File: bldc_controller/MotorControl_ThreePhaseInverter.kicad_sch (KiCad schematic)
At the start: 42 parts, among them J11 Phase A, J12 Phase B, J13 Phase C

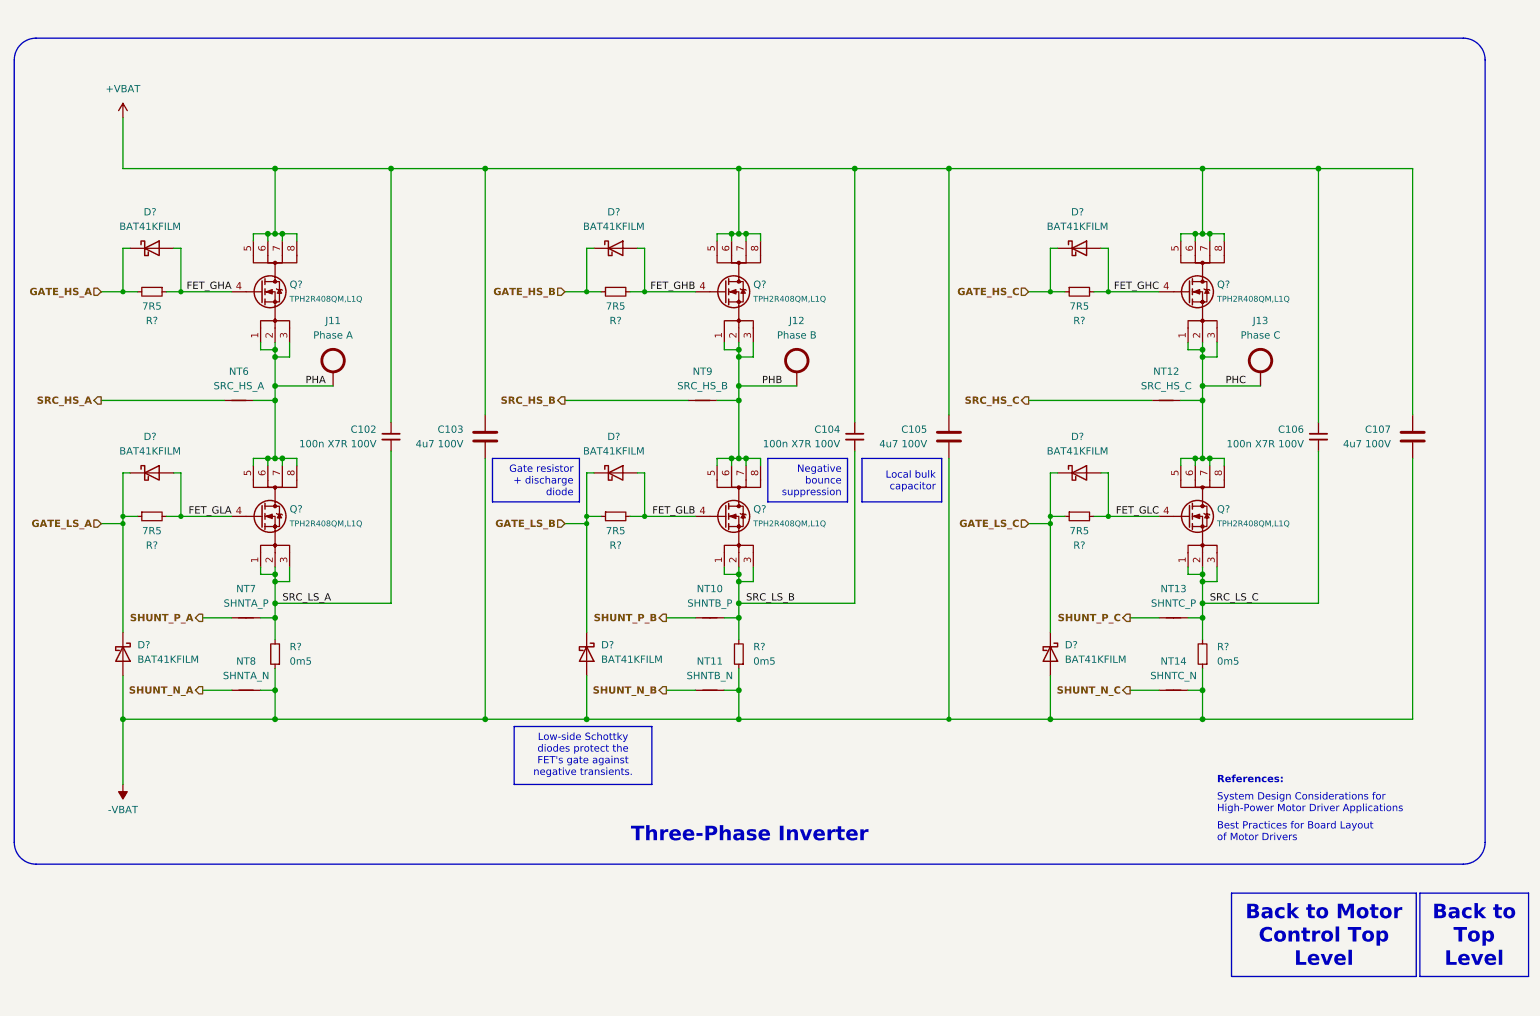
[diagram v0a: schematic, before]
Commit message: added IPC-7351 compliant footprints and started routing
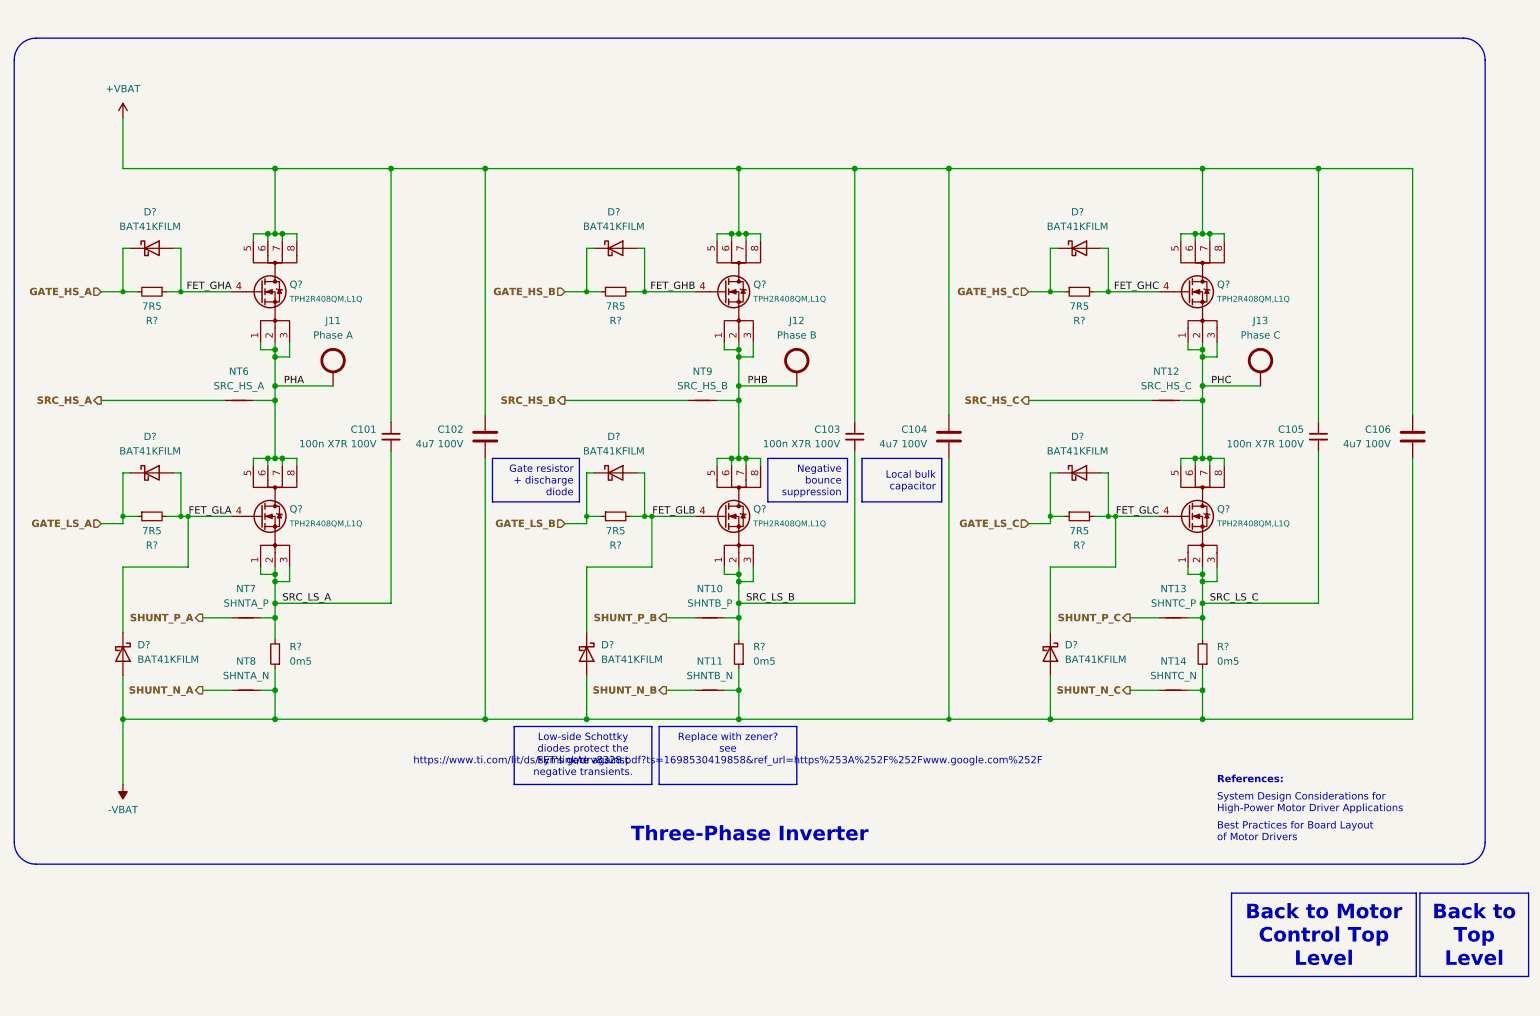
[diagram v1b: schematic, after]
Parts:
- C101: renamed from C102; footprint (none) -> 0_capacitor_smd:C_1206_3216_DensityHighest
- C102: renamed from C103; footprint Capacitor_SMD:C_1206_3216Metric -> 0_capacitor_smd:C_1206_3216_DensityHighest
- C103: renamed from C104; footprint (none) -> 0_capacitor_smd:C_1206_3216_DensityHighest
- C104: renamed from C105; footprint Capacitor_SMD:C_1206_3216Metric -> 0_capacitor_smd:C_1206_3216_DensityHighest
- C105: renamed from C106; footprint (none) -> 0_capacitor_smd:C_1206_3216_DensityHighest
- C106: renamed from C107; footprint Capacitor_SMD:C_1206_3216Metric -> 0_capacitor_smd:C_1206_3216_DensityHighest
- NT10, NT11, NT13, NT14, NT7, NT8: footprint NetTie:NetTie-2_SMD_Pad0.5mm -> 0_net_tie:NetTie-2_SMD_Pad0.2mm
- NT12, NT6, NT9: footprint NetTie:NetTie-2_SMD_Pad0.5mm -> 0_net_tie:NetTie-2_SMD_Pad0.4mm
- R? (x3): footprint Resistor_SMD:R_1206_3216Metric -> 0_resistor_smd:R_1206_3216_DensityHigh
- R? (x6): footprint Resistor_SMD:R_0805_2012Metric -> 0_resistor_smd:R_0805_2012_DensityHigh
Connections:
- net FET_GLA: now also D?.1 (K)
- net FET_GLB: now also D?.1 (K)
- net FET_GLC: now also D?.1 (K)
- net GATE_LS_A: no longer D?.1 (K)
- net GATE_LS_B: no longer D?.1 (K)
- net GATE_LS_C: no longer D?.1 (K)

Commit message: some progress on the pcb
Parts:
- C103: footprint 0_capacitor_smd:C_1206_3216_DensityHighest -> 0_capacitor_smd:C_0805_2012_DensityHigh
- D?: footprint Diode_SMD:D_SOD-523 -> 0_diode_smd:D_SOD-523_Spaced
- J11, J12, J13: footprint MountingHole:MountingHole_5mm_Pad_Via -> 0_pad:Pad_Square_Vias_6.5x6.5mm
- NT12, NT6, NT9: footprint 0_net_tie:NetTie-2_SMD_Pad0.4mm -> 0_net_tie:NetTie-2_SMD_Pad0.3mm
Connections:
- net -VBAT renamed GND
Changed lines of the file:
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@@
       (effects (font (size 1.27 1.27)))
     )
-    (property "Footprint" "0_net_tie:NetTie-2_SMD_Pad0.4mm" (at 220.98 80.01 0)
+    (property "Footprint" "0_net_tie:NetTie-2_SMD_Pad0.3mm" (at 220.98 80.01 0)
       (effects (font (size 1.27 1.27)) hide)
     )
@@
       (effects (font (size 1.27 1.27)))
     )
-    (property "Footprint" "0_net_tie:NetTie-2_SMD_Pad0.4mm" (at 58.42 80.01 0)
+    (property "Footprint" "0_net_tie:NetTie-2_SMD_Pad0.3mm" (at 58.42 80.01 0)
       (effects (font (size 1.27 1.27)) hide)
     )
@@
       (effects (font (size 1.27 1.27)) (justify left))
     )
-    (property "Footprint" "0_capacitor_smd:C_1206_3216_DensityHighest" (at 166.37 86.36 0)
+    (property "Footprint" "0_capacitor_smd:C_0805_2012_DensityHigh" (at 166.37 86.36 0)
       (effects (font (size 1.27 1.27)) hide)
     )
@@
     )
   )
-  (symbol (lib_id "0_power_symbols:-VBAT") (at 38.1 147.32 180) (unit 1)
-    (in_bom yes) (on_board yes) (dnp no) (fields_autoplaced)
-    (property "Reference" "#PWR?" (at 38.1 149.86 0)
-      (effects (font (size 1.27 1.27)) hide)
-    )
-    (property "Value" "-VBAT" (at 38.1 151.765 0)
+  (symbol (lib_id "0_diode:BAT41KFILM") (at 205.74 53.34 0) (unit 1)
+    (in_bom yes) (on_board yes) (dnp no) (fields_autoplaced)
+    (property "Reference" "D?" (at 205.4225 46.99 0)
+      (effects (font (size 1.27 1.27)))
+    )
+    (property "Value" "BAT41KFILM" (at 205.4225 49.53 0)
+      (effects (font (size 1.27 1.27)))
+    )
+    (property "Footprint" "Diode_SMD:D_SOD-523" (at 205.74 57.785 0)
+      (effects (font (size 1.27 1.27)) hide)
+    )
+    (property "Datasheet" "https://www.mouser.ch/datasheet/2/389/bat41-1848934.pdf" (at 205.74 53.34 0)
+      (effects (font (size 1.27 1.27)) hide)
+    )
+    (pin "1")
+    (pin "2")
+    (instances
+      (project "bldc_controller"
+        (path "/0650c7a8-acba-429c-9f8e-eec0baf0bc1c/a6223e2e-2896-4182-b4ad-55a63bc87f3d"
+          (reference "D?") (unit 1)
+        )
+        (path "/0650c7a8-acba-429c-9f8e-eec0baf0bc1c/a6223e2e-2896-4182-b4ad-55a63bc87f3d/4a9c9b06-3536-46ef-a76d-6cac03a1fe38"
+          (reference "D13") (unit 1)
+        )
+      )
+    )
+  )
+  (symbol (lib_id "0_diode:BAT41KFILM") (at 200.66 124.46 270) (unit 1)
+    (in_bom yes) (on_board yes) (dnp no) (fields_autoplaced)
+    (property "Reference" "D?" (at 203.2 122.8725 90)
+      (effects (font (size 1.27 1.27)) (justify left))
+    )
+    (property "Value" "BAT41KFILM" (at 203.2 125.4125 90)
+      (effects (font (size 1.27 1.27)) (justify left))
+    )
+    (property "Footprint" "Diode_SMD:D_SOD-523" (at 196.215 124.46 0)
+      (effects (font (size 1.27 1.27)) hide)
+    )
+    (property "Datasheet" "https://www.mouser.ch/datasheet/2/389/bat41-1848934.pdf" (at 200.66 124.46 0)
+      (effects (font (size 1.27 1.27)) hide)
+    )
+    (pin "1")
+    (pin "2")
+    (instances
+      (project "bldc_controller"
+        (path "/0650c7a8-acba-429c-9f8e-eec0baf0bc1c/a6223e2e-2896-4182-b4ad-55a63bc87f3d"
+          (reference "D?") (unit 1)
+        )
+        (path "/0650c7a8-acba-429c-9f8e-eec0baf0bc1c/a6223e2e-2896-4182-b4ad-55a63bc87f3d/4a9c9b06-3536-46ef-a76d-6cac03a1fe38"
+          (reference "D12") (unit 1)
+        )
+      )
+    )
+  )
+  (symbol (lib_id "Device:R_Small") (at 205.74 100.33 90) (mirror x) (unit 1)
+    (in_bom yes) (on_board yes) (dnp no)
+    (property "Reference" "R?" (at 205.74 105.41 90)
+      (effects (font (size 1.27 1.27)))
+    )
+    (property "Value" "7R5" (at 205.74 102.87 90)
+      (effects (font (size 1.27 1.27)))
+    )
+    (property "Footprint" "0_resistor_smd:R_0805_2012_DensityHigh" (at 205.74 100.33 0)
+      (effects (font (size 1.27 1.27)) hide)
+    )
+    (property "Datasheet" "~" (at 205.74 100.33 0)
+      (effects (font (size 1.27 1.27)) hide)
+    )
+    (pin "1")
+    (pin "2")
+    (instances
+      (project "bldc_controller"
+        (path "/0650c7a8-acba-429c-9f8e-eec0baf0bc1c/a6223e2e-2896-4182-b4ad-55a63bc87f3d"
+          (reference "R?") (unit 1)
+        )
+        (path "/0650c7a8-acba-429c-9f8e-eec0baf0bc1c/a6223e2e-2896-4182-b4ad-55a63bc87f3d/4a9c9b06-3536-46ef-a76d-6cac03a1fe38"
+          (reference "R39") (unit 1)
+        )
+      )
+    )
+  )
+  (symbol (lib_id "power:GND") (at 38.1 147.32 0) (unit 1)
+    (in_bom yes) (on_board yes) (dnp no) (fields_autoplaced)
+    (property "Reference" "#PWR07" (at 38.1 153.67 0)
+      (effects (font (size 1.27 1.27)) hide)
+    )
+    (property "Value" "GND" (at 38.1 152.4 0)
       (effects (font (size 1.27 1.27)))
     )
@@
     (instances
       (project "bldc_controller"
-        (path "/0650c7a8-acba-429c-9f8e-eec0baf0bc1c/a6223e2e-2896-4182-b4ad-55a63bc87f3d"
-          (reference "#PWR?") (unit 1)
+        (path "/0650c7a8-acba-429c-9f8e-eec0baf0bc1c/b89a7d22-bda3-4776-b5ce-8f6b0eb8f2a5"
+          (reference "#PWR07") (unit 1)
         )
         (path "/0650c7a8-acba-429c-9f8e-eec0baf0bc1c/a6223e2e-2896-4182-b4ad-55a63bc87f3d/4a9c9b06-3536-46ef-a76d-6cac03a1fe38"
@@
     )
   )
-  (symbol (lib_id "0_diode:BAT41KFILM") (at 205.74 53.34 0) (unit 1)
-    (in_bom yes) (on_board yes) (dnp no) (fields_autoplaced)
-    (property "Reference" "D?" (at 205.4225 46.99 0)
-      (effects (font (size 1.27 1.27)))
-    )
-    (property "Value" "BAT41KFILM" (at 205.4225 49.53 0)
-      (effects (font (size 1.27 1.27)))
-    )
-    (property "Footprint" "Diode_SMD:D_SOD-523" (at 205.74 57.785 0)
-      (effects (font (size 1.27 1.27)) hide)
-    )
-    (property "Datasheet" "https://www.mouser.ch/datasheet/2/389/bat41-1848934.pdf" (at 205.74 53.34 0)
-      (effects (font (size 1.27 1.27)) hide)
-    )
-    (pin "1")
-    (pin "2")
-    (instances
-      (project "bldc_controller"
-        (path "/0650c7a8-acba-429c-9f8e-eec0baf0bc1c/a6223e2e-2896-4182-b4ad-55a63bc87f3d"
-          (reference "D?") (unit 1)
-        )
-        (path "/0650c7a8-acba-429c-9f8e-eec0baf0bc1c/a6223e2e-2896-4182-b4ad-55a63bc87f3d/4a9c9b06-3536-46ef-a76d-6cac03a1fe38"
-          (reference "D13") (unit 1)
-        )
-      )
-    )
-  )
-  (symbol (lib_id "0_diode:BAT41KFILM") (at 200.66 124.46 270) (unit 1)
-    (in_bom yes) (on_board yes) (dnp no) (fields_autoplaced)
-    (property "Reference" "D?" (at 203.2 122.8725 90)
-      (effects (font (size 1.27 1.27)) (justify left))
-    )
-    (property "Value" "BAT41KFILM" (at 203.2 125.4125 90)
-      (effects (font (size 1.27 1.27)) (justify left))
-    )
-    (property "Footprint" "Diode_SMD:D_SOD-523" (at 196.215 124.46 0)
-      (effects (font (size 1.27 1.27)) hide)
-    )
-    (property "Datasheet" "https://www.mouser.ch/datasheet/2/389/bat41-1848934.pdf" (at 200.66 124.46 0)
-      (effects (font (size 1.27 1.27)) hide)
-    )
-    (pin "1")
-    (pin "2")
-    (instances
-      (project "bldc_controller"
-        (path "/0650c7a8-acba-429c-9f8e-eec0baf0bc1c/a6223e2e-2896-4182-b4ad-55a63bc87f3d"
-          (reference "D?") (unit 1)
-        )
-        (path "/0650c7a8-acba-429c-9f8e-eec0baf0bc1c/a6223e2e-2896-4182-b4ad-55a63bc87f3d/4a9c9b06-3536-46ef-a76d-6cac03a1fe38"
-          (reference "D12") (unit 1)
-        )
-      )
-    )
-  )
-  (symbol (lib_id "Device:R_Small") (at 205.74 100.33 90) (mirror x) (unit 1)
-    (in_bom yes) (on_board yes) (dnp no)
-    (property "Reference" "R?" (at 205.74 105.41 90)
-      (effects (font (size 1.27 1.27)))
-    )
-    (property "Value" "7R5" (at 205.74 102.87 90)
-      (effects (font (size 1.27 1.27)))
-    )
-    (property "Footprint" "0_resistor_smd:R_0805_2012_DensityHigh" (at 205.74 100.33 0)
-      (effects (font (size 1.27 1.27)) hide)
-    )
-    (property "Datasheet" "~" (at 205.74 100.33 0)
-      (effects (font (size 1.27 1.27)) hide)
-    )
-    (pin "1")
-    (pin "2")
-    (instances
-      (project "bldc_controller"
-        (path "/0650c7a8-acba-429c-9f8e-eec0baf0bc1c/a6223e2e-2896-4182-b4ad-55a63bc87f3d"
-          (reference "R?") (unit 1)
-        )
-        (path "/0650c7a8-acba-429c-9f8e-eec0baf0bc1c/a6223e2e-2896-4182-b4ad-55a63bc87f3d/4a9c9b06-3536-46ef-a76d-6cac03a1fe38"
-          (reference "R39") (unit 1)
-        )
-      )
-    )
-  )
   (symbol (lib_id "0_connectors:Solder Pad") (at 237.49 77.47 0) (unit 1)
     (in_bom yes) (on_board yes) (dnp no)
@@
       (effects (font (size 1.27 1.27)))
     )
-    (property "Footprint" "MountingHole:MountingHole_5mm_Pad_Via" (at 242.57 77.47 0)
+    (property "Footprint" "0_pad:Pad_Square_Vias_6.5x6.5mm" (at 242.57 77.47 0)
       (effects (font (size 1.27 1.27)) hide)
     )
@@
       (effects (font (size 1.27 1.27)))
     )
-    (property "Footprint" "Diode_SMD:D_SOD-523" (at 124.46 97.155 0)
+    (property "Footprint" "0_diode_smd:D_SOD-523_Spaced" (at 124.46 97.155 0)
       (effects (font (size 1.27 1.27)) hide)
     )
@@
       (effects (font (size 1.27 1.27)))
     )
-    (property "Footprint" "MountingHole:MountingHole_5mm_Pad_Via" (at 80.01 77.47 0)
+    (property "Footprint" "0_pad:Pad_Square_Vias_6.5x6.5mm" (at 80.01 77.47 0)
       (effects (font (size 1.27 1.27)) hide)
     )
@@
       (effects (font (size 1.27 1.27)))
     )
-    (property "Footprint" "0_net_tie:NetTie-2_SMD_Pad0.4mm" (at 139.7 80.01 0)
+    (property "Footprint" "0_net_tie:NetTie-2_SMD_Pad0.3mm" (at 139.7 80.01 0)
       (effects (font (size 1.27 1.27)) hide)
     )
@@
       (effects (font (size 1.27 1.27)))
     )
-    (property "Footprint" "MountingHole:MountingHole_5mm_Pad_Via" (at 161.29 77.47 0)
-      (effects (font (size 1.27 1.27)) hide)
-    )
+    (property "Footprint" "0_pad:Pad_Square_Vias_6.5x6.5mm" (at 161.29 77.47 0)
+      (effects (font (size 1.27 1.27)) hide)
+    )

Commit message: Added TVS diodes to all interfaces
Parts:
- D?: footprint 0_diode_smd:D_SOD-523_Spaced -> Diode_SMD:D_SOD-523
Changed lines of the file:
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@@
       (effects (font (size 1.27 1.27)))
     )
-    (property "Footprint" "0_diode_smd:D_SOD-523_Spaced" (at 124.46 97.155 0)
+    (property "Footprint" "Diode_SMD:D_SOD-523" (at 124.46 97.155 0)
       (effects (font (size 1.27 1.27)) hide)
     )

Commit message: might have fixed net issue, added dxf and svgs
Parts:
- gave numbers to parts that had none: 24
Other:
- moved on the sheet: C101, C102, C103, C104, C105, C106, D10, D11, D12, D13, D14, D6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

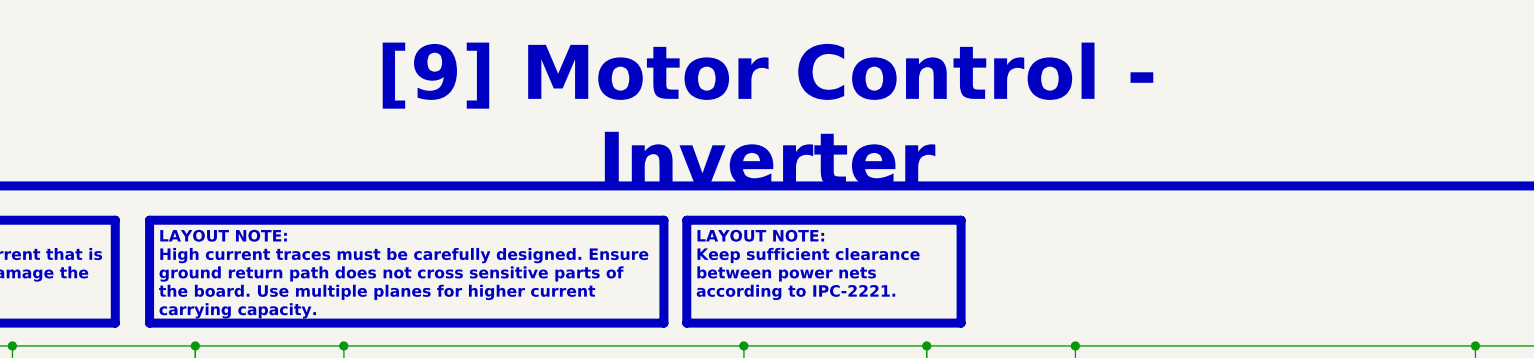
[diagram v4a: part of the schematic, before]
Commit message: Replaced 3v3 buck with WSON package alternative. Will back-annotate components
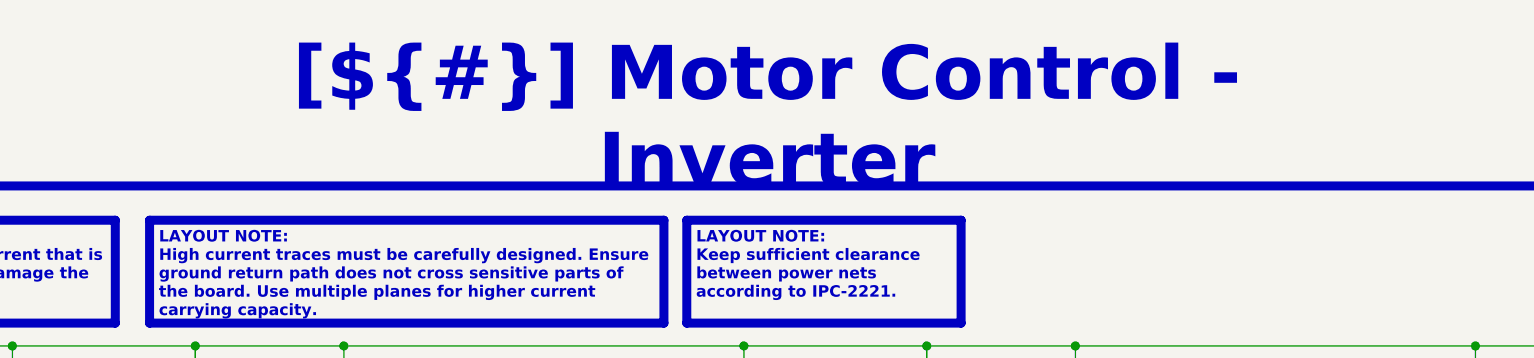
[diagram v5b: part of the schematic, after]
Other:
- company: EPFL Xplore -> ${COMPANY}
- title: Three Phase Driver -> Motor Control - Inverter
